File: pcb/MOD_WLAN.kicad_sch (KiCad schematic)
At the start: 8 parts, among them IC2 ESP32-C6-WROOM-1-N8, SW1 SW_DIP_x01

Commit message: updated wlan
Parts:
- added JP4, JP5: SolderJumper_2_Open, Jumper:SolderJumper-2_P1.3mm_Open_RoundedPad1.0x1.5mm, symbol Jumper:SolderJumper_2_Open
- added R53, R54: 100R, Resistor_SMD:R_0603_1608Metric_Pad0.98x0.95mm_HandSolder, symbol Device:R
- added R57: 10k, Resistor_SMD:R_0603_1608Metric_Pad0.98x0.95mm_HandSolder, symbol Device:R
- added R58, R59, R60, R72: 22R, Resistor_SMD:R_0603_1608Metric_Pad0.98x0.95mm_HandSolder, symbol Device:R
- added TP16: WLAN_EN, TestPoint:TestPoint_THTPad_D2.0mm_Drill1.0mm, symbol Connector:TestPoint
- added TP17: WLAN_BOOT, TestPoint:TestPoint_THTPad_D2.0mm_Drill1.0mm, symbol Connector:TestPoint
- C50: value 10u -> 22uF
- R47: value 100k -> 10k
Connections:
- net 3V3: now also R57.1
- net ESP_BOOT: now also JP5.1 (A); no longer IC2.15 (IO9), R47.2
- net ESP_EN: now also JP4.1 (A); no longer C48.1, IC2.3 (EN), R48.2, SW1.1
- net ESP_RX: now also R54.2; no longer IC2.24 (RXD0)
- net ESP_SPI_CLK: now also R58.1; no longer IC2.6 (IO6)
- net ESP_SPI_CS: now also R57.2, R60.1; no longer IC2.16 (IO18)
- net ESP_SPI_MISO: now also R72.2; no longer IC2.27 (IO2)
- net ESP_SPI_MOSI: now also R59.1; no longer IC2.7 (IO7)
- net ESP_TX: now also R53.2; no longer IC2.25 (TXD0)
- new net: IC2.24 (RXD0), R53.1
- new net: IC2.7 (IO7), R59.2
- new net: C48.1, IC2.3 (EN), JP4.2 (B), R48.2, SW1.1, TP16.1
- new net: IC2.6 (IO6), R58.2
- new net: IC2.15 (IO9), JP5.2 (B), R47.2, TP17.1
- new net: IC2.25 (TXD0), R54.1
- new net: IC2.16 (IO18), R60.2
- new net: IC2.27 (IO2), R72.1
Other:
- moved on the sheet: R49

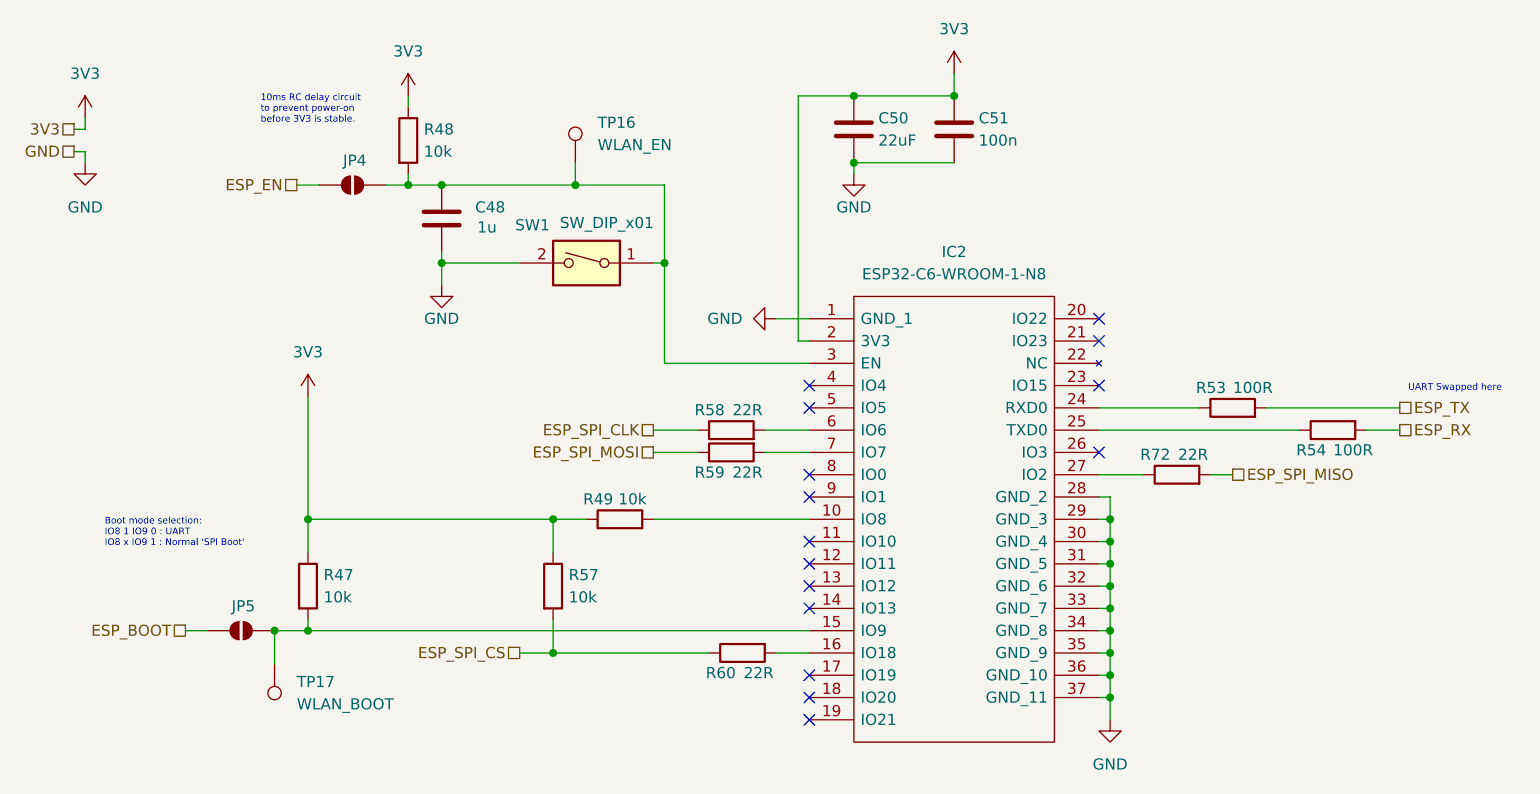
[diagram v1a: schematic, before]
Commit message: reannotated, updated some symbols
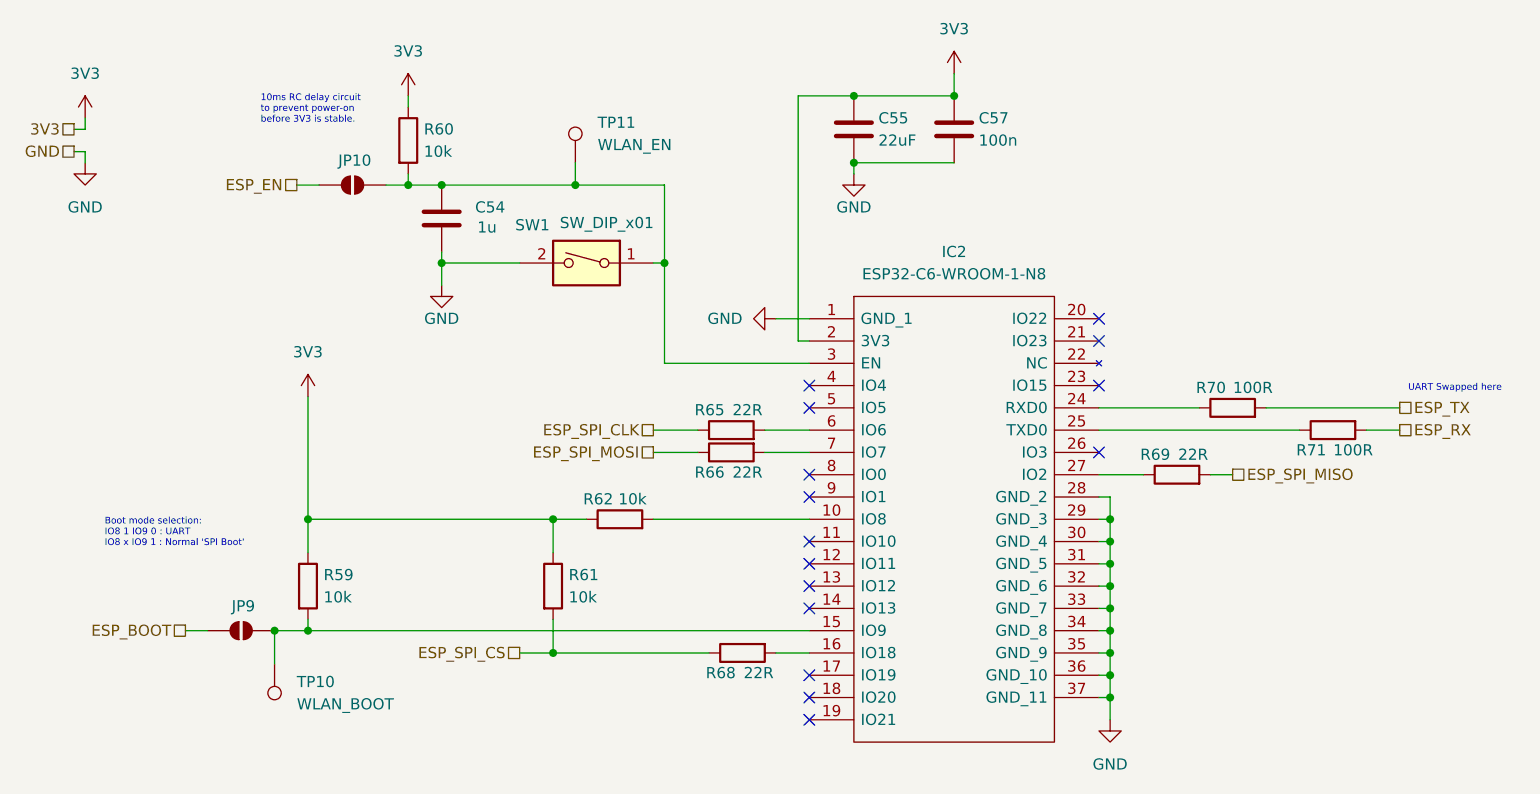
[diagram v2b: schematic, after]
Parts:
- renumbered C48 to C54, C50 to C55, C51 to C57, JP4 to JP10, JP5 to JP9, R47 to R59, R48 to R60, R57 to R61, R49 to R62, R58 to R65, R59 to R66, R60 to R68, R72 to R69, R53 to R70, R54 to R71, TP17 to TP10, TP16 to TP11
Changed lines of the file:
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@@
 		(on_board yes)
 		(dnp no)
-		(property "Reference" "R53"
+		(property "Reference" "R70"
 			(at 156.718 54.864 90)
 			(effects
@@
 			(project "NCU"
 				(path "/3aee14c3-5480-4f7c-989e-3fef81779034/0cdbc80d-6682-4488-acea-b93c92a9f88d"
-					(reference "R53")
+					(reference "R70")
 					(unit 1)
 				)
@@
 		(on_board yes)
 		(dnp no)
-		(property "Reference" "R59"
+		(property "Reference" "R66"
 			(at 99.568 64.516 90)
 			(effects
@@
 			(project "NCU"
 				(path "/3aee14c3-5480-4f7c-989e-3fef81779034/0cdbc80d-6682-4488-acea-b93c92a9f88d"
-					(reference "R59")
+					(reference "R66")
 					(unit 1)
 				)
@@
 		(on_board yes)
 		(dnp no)
-		(property "Reference" "R49"
+		(property "Reference" "R62"
 			(at 86.868 67.564 90)
 			(effects
@@
 			(project "NCU"
 				(path "/3aee14c3-5480-4f7c-989e-3fef81779034/0cdbc80d-6682-4488-acea-b93c92a9f88d"
-					(reference "R49")
+					(reference "R62")
 					(unit 1)
 				)
@@
 		(on_board yes)
 		(dnp no)
-		(property "Reference" "#PWR0218"
+		(property "Reference" "#PWR0286"
 			(at 114.3 36.83 0)
 			(effects
@@
 			(project "NCU"
 				(path "/3aee14c3-5480-4f7c-989e-3fef81779034/0cdbc80d-6682-4488-acea-b93c92a9f88d"
-					(reference "#PWR0218")
+					(reference "#PWR0286")
 					(unit 1)
 				)
@@
 		(on_board yes)
 		(dnp no)
-		(property "Reference" "R48"
+		(property "Reference" "R60"
 			(at 65.278 25.4 0)
 			(effects
@@
 			(project "NCU"
 				(path "/3aee14c3-5480-4f7c-989e-3fef81779034/0cdbc80d-6682-4488-acea-b93c92a9f88d"
-					(reference "R48")
+					(reference "R60")
 					(unit 1)
 				)
@@
 		(dnp no)
 		(fields_autoplaced yes)
-		(property "Reference" "#PWR0209"
+		(property "Reference" "#PWR0278"
 			(at 26.67 27.94 0)
 			(effects
@@
 			(project "NCU"
 				(path "/3aee14c3-5480-4f7c-989e-3fef81779034/0cdbc80d-6682-4488-acea-b93c92a9f88d"
-					(reference "#PWR0209")
+					(reference "#PWR0278")
 					(unit 1)
 				)
@@
 		(on_board yes)
 		(dnp no)
-		(property "Reference" "R58"
+		(property "Reference" "R65"
 			(at 99.568 57.404 90)
 			(effects
@@
 			(project "NCU"
 				(path "/3aee14c3-5480-4f7c-989e-3fef81779034/0cdbc80d-6682-4488-acea-b93c92a9f88d"
-					(reference "R58")
+					(reference "R65")
 					(unit 1)
 				)
@@
 		(on_board yes)
 		(dnp no)
-		(property "Reference" "R47"
+		(property "Reference" "R59"
 			(at 53.848 76.2 0)
 			(effects
@@
 			(project "NCU"
 				(path "/3aee14c3-5480-4f7c-989e-3fef81779034/0cdbc80d-6682-4488-acea-b93c92a9f88d"
-					(reference "R47")
+					(reference "R59")
 					(unit 1)
 				)
@@
 		(on_board yes)
 		(dnp no)
-		(property "Reference" "R54"
+		(property "Reference" "R71"
 			(at 168.148 61.976 90)
 			(effects
@@
 			(project "NCU"
 				(path "/3aee14c3-5480-4f7c-989e-3fef81779034/0cdbc80d-6682-4488-acea-b93c92a9f88d"
-					(reference "R54")
+					(reference "R71")
 					(unit 1)
 				)
@@
 		(dnp no)
 		(fields_autoplaced yes)
-		(property "Reference" "TP16"
+		(property "Reference" "TP11"
 			(at 85.09 24.6379 0)
 			(effects
@@
 			(project "NCU"
 				(path "/3aee14c3-5480-4f7c-989e-3fef81779034/0cdbc80d-6682-4488-acea-b93c92a9f88d"
-					(reference "TP16")
+					(reference "TP11")
 					(unit 1)
 				)
@@
 		(on_board yes)
 		(dnp no)
-		(property "Reference" "JP4"
+		(property "Reference" "JP10"
 			(at 57.404 28.956 0)
 			(effects
@@
 			(project ""
 				(path "/3aee14c3-5480-4f7c-989e-3fef81779034/0cdbc80d-6682-4488-acea-b93c92a9f88d"
-					(reference "JP4")
+					(reference "JP10")
 					(unit 1)
 				)
@@
 		(on_board yes)
 		(dnp no)
-		(property "Reference" "C48"
+		(property "Reference" "C54"
 			(at 71.12 34.2899 0)
 			(effects
@@
 			(project ""
 				(path "/3aee14c3-5480-4f7c-989e-3fef81779034/0cdbc80d-6682-4488-acea-b93c92a9f88d"
-					(reference "C48")
+					(reference "C54")
 					(unit 1)
 				)
@@
 		(dnp no)
 		(fields_autoplaced yes)
-		(property "Reference" "#PWR0219"
+		(property "Reference" "#PWR0288"
 			(at 125.73 22.86 0)
 			(effects
@@
 			(project "NCU"
 				(path "/3aee14c3-5480-4f7c-989e-3fef81779034/0cdbc80d-6682-4488-acea-b93c92a9f88d"
-					(reference "#PWR0219")
+					(reference "#PWR0288")
 					(unit 1)
 				)
@@
 		(dnp no)
 		(fields_autoplaced yes)
-		(property "Reference" "#PWR0213"
+		(property "Reference" "#PWR0282"
 			(at 63.5 25.4 0)
 			(effects
@@
 			(project "NCU"
 				(path "/3aee14c3-5480-4f7c-989e-3fef81779034/0cdbc80d-6682-4488-acea-b93c92a9f88d"
-					(reference "#PWR0213")
+					(reference "#PWR0282")
 					(unit 1)
 				)
@@
 		(dnp no)
 		(fields_autoplaced yes)
-		(property "Reference" "#PWR0220"
+		(property "Reference" "#PWR0291"
 			(at 143.51 99.06 0)
 			(effects
@@
 			(project "NCU"
 				(path "/3aee14c3-5480-4f7c-989e-3fef81779034/0cdbc80d-6682-4488-acea-b93c92a9f88d"
-					(reference "#PWR0220")
+					(reference "#PWR0291")
 					(unit 1)
 				)
@@
 		(dnp no)
 		(fields_autoplaced yes)
-		(property "Reference" "TP17"
+		(property "Reference" "TP10"
 			(at 50.8 88.3919 0)
 			(effects
@@
 			(project "NCU"
 				(path "/3aee14c3-5480-4f7c-989e-3fef81779034/0cdbc80d-6682-4488-acea-b93c92a9f88d"
-					(reference "TP17")
+					(reference "TP10")
 					(unit 1)
 				)
@@
 		(on_board yes)
 		(dnp no)
-		(property "Reference" "C50"
+		(property "Reference" "C55"
 			(at 117.094 24.13 0)
 			(effects
@@
 			(project "NCU"
 				(path "/3aee14c3-5480-4f7c-989e-3fef81779034/0cdbc80d-6682-4488-acea-b93c92a9f88d"
-					(reference "C50")
+					(reference "C55")
 					(unit 1)
 				)
@@
 		(dnp no)
 		(fields_autoplaced yes)
-		(property "Reference" "#PWR0216"
+		(property "Reference" "#PWR0285"
 			(at 99.06 46.99 0)
 			(effects
@@
 			(project "NCU"
 				(path "/3aee14c3-5480-4f7c-989e-3fef81779034/0cdbc80d-6682-4488-acea-b93c92a9f88d"
-					(reference "#PWR0216")
+					(reference "#PWR0285")
 					(unit 1)
 				)
@@
 		(on_board yes)
 		(dnp no)
-		(property "Reference" "#PWR0214"
+		(property "Reference" "#PWR0283"
 			(at 67.31 49.53 0)
 			(effects
@@
 			(project "NCU"
 				(path "/3aee14c3-5480-4f7c-989e-3fef81779034/0cdbc80d-6682-4488-acea-b93c92a9f88d"
-					(reference "#PWR0214")
+					(reference "#PWR0283")
 					(unit 1)
 				)
@@
 		(on_board yes)
 		(dnp no)
-		(property "Reference" "R60"
+		(property "Reference" "R68"
 			(at 100.838 87.376 90)
 			(effects
@@
 			(project "NCU"
 				(path "/3aee14c3-5480-4f7c-989e-3fef81779034/0cdbc80d-6682-4488-acea-b93c92a9f88d"
-					(reference "R60")
+					(reference "R68")
 					(unit 1)
 				)
@@
 		(on_board yes)
 		(dnp no)
-		(property "Reference" "R57"
+		(property "Reference" "R61"
 			(at 81.788 76.2 0)
 			(effects
@@
 			(project "NCU"
 				(path "/3aee14c3-5480-4f7c-989e-3fef81779034/0cdbc80d-6682-4488-acea-b93c92a9f88d"
-					(reference "R57")
+					(reference "R61")
 					(unit 1)
 				)
@@
 		(dnp no)
 		(fields_autoplaced yes)
-		(property "Reference" "#PWR0212"
+		(property "Reference" "#PWR0281"
 			(at 52.07 59.69 0)
 			(effects
@@
 			(project "NCU"
 				(path "/3aee14c3-5480-4f7c-989e-3fef81779034/0cdbc80d-6682-4488-acea-b93c92a9f88d"
-					(reference "#PWR0212")
+					(reference "#PWR0281")
 					(unit 1)
 				)
@@
 		(on_board yes)
 		(dnp no)
-		(property "Reference" "R72"
+		(property "Reference" "R69"
 			(at 150.368 62.484 90)
 			(effects
@@
 			(project "NCU"
 				(path "/3aee14c3-5480-4f7c-989e-3fef81779034/0cdbc80d-6682-4488-acea-b93c92a9f88d"
-					(reference "R72")
+					(reference "R69")
 					(unit 1)
 				)
@@
 		(on_board yes)
 		(dnp no)
-		(property "Reference" "JP5"
+		(property "Reference" "JP9"
 			(at 44.704 79.756 0)
 			(effects
@@
 			(project "NCU"
 				(path "/3aee14c3-5480-4f7c-989e-3fef81779034/0cdbc80d-6682-4488-acea-b93c92a9f88d"
-					(reference "JP5")
+					(reference "JP9")
 					(unit 1)
 				)
@@
 		(dnp no)
 		(fields_autoplaced yes)
-		(property "Reference" "#PWR0211"
+		(property "Reference" "#PWR0280"
 			(at 26.67 35.56 0)
 			(effects
@@
 			(project "NCU"
 				(path "/3aee14c3-5480-4f7c-989e-3fef81779034/0cdbc80d-6682-4488-acea-b93c92a9f88d"
-					(reference "#PWR0211")
+					(reference "#PWR0280")
 					(unit 1)
 				)
@@
 		(on_board yes)
 		(dnp no)
-		(property "Reference" "C51"
+		(property "Reference" "C57"
 			(at 128.524 24.13 0)
 			(effects
@@
 			(project "NCU"
 				(path "/3aee14c3-5480-4f7c-989e-3fef81779034/0cdbc80d-6682-4488-acea-b93c92a9f88d"
-					(reference "C51")
-					(unit 1)
-				)
+					(reference "C57")
+					(unit 1)
+				)

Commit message: minor changes before layout
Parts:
- added TP21: ESP_TX, TestPoint:TestPoint_THTPad_D2.0mm_Drill1.0mm, symbol Connector:TestPoint
- added TP22: ESP_RX, TestPoint:TestPoint_THTPad_D2.0mm_Drill1.0mm, symbol Connector:TestPoint
- C55: value 22uF -> 47uF
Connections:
- net ESP_RX: now also TP22.1
- net ESP_TX: now also TP21.1
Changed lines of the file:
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@@
+	)
+	(junction
+		(at 175.26 57.15)
+		(diameter 0)
+		(color 0 0 0 0)
 	)
 	(junction
@@
 	)
 	(junction
+		(at 175.26 59.69)
+		(diameter 0)
+		(color 0 0 0 0)
+	)
+	(junction
 		(at 143.51 87.63)
 		(diameter 0)
@@
 	(wire
 		(pts
+			(xy 175.26 53.34) (xy 175.26 57.15)
+		)
+		(stroke
+			(width 0)
+			(type default)
+		)
+	)
+	(wire
+		(pts
 			(xy 63.5 21.59) (xy 63.5 22.86)
 		)
@@
 	(wire
 		(pts
-			(xy 172.72 59.69) (xy 176.53 59.69)
+			(xy 172.72 59.69) (xy 175.26 59.69)
 		)
 		(stroke
@@
 	(wire
 		(pts
+			(xy 175.26 59.69) (xy 176.53 59.69)
+		)
+		(stroke
+			(width 0)
+			(type default)
+		)
+	)
+	(wire
+		(pts
 			(xy 142.24 57.15) (xy 153.67 57.15)
 		)
@@
 	(wire
 		(pts
+			(xy 175.26 57.15) (xy 176.53 57.15)
+		)
+		(stroke
+			(width 0)
+			(type default)
+		)
+	)
+	(wire
+		(pts
 			(xy 52.07 69.85) (xy 52.07 73.66)
 		)
@@
 	(wire
 		(pts
-			(xy 161.29 57.15) (xy 176.53 57.15)
+			(xy 161.29 57.15) (xy 175.26 57.15)
 		)
 		(stroke
@@
 		(pts
 			(xy 67.31 31.75) (xy 82.55 31.75)
+		)
+		(stroke
+			(width 0)
+			(type default)
+		)
+	)
+	(wire
+		(pts
+			(xy 175.26 59.69) (xy 175.26 62.23)
 		)
 		(stroke
@@
 			)
 		)
-		(property "Value" "22uF"
+		(property "Value" "47uF"
 			(at 117.094 26.67 0)
 			(effects
@@
 	)
 	(symbol
+		(lib_id "Connector:TestPoint")
+		(at 175.26 62.23 0)
+		(mirror x)
+		(unit 1)
+		(exclude_from_sim no)
+		(in_bom yes)
+		(on_board yes)
+		(dnp no)
+		(property "Reference" "TP22"
+			(at 177.8 66.8021 0)
+			(effects
+				(font
+					(size 1.27 1.27)
+				)
+				(justify left)
+			)
+		)
+		(property "Value" "ESP_RX"
+			(at 177.8 64.2621 0)
+			(effects
+				(font
+					(size 1.27 1.27)
+				)
+				(justify left)
+			)
+		)
+		(property "Footprint" "TestPoint:TestPoint_THTPad_D2.0mm_Drill1.0mm"
+			(at 180.34 62.23 0)
+			(effects
+				(font
+					(size 1.27 1.27)
+				)
+				(hide yes)
+			)
+		)
+		(property "Datasheet" "~"
+			(at 180.34 62.23 0)
+			(effects
+				(font
+					(size 1.27 1.27)
+				)
+				(hide yes)
+			)
+		)
+		(property "Description" "test point"
+			(at 175.26 62.23 0)
+			(effects
+				(font
+					(size 1.27 1.27)
+				)
+				(hide yes)
+			)
+		)
+		(pin "1"
+		)
+		(instances
+			(project "NCU"
+				(path "/3aee14c3-5480-4f7c-989e-3fef81779034/0cdbc80d-6682-4488-acea-b93c92a9f88d"
+					(reference "TP22")
+					(unit 1)
+				)
+			)
+		)
+	)
+	(symbol
 		(lib_id "Device:R")
 		(at 80.01 77.47 0)
@@
 					(unit 1)
 				)
+			)
+		)
+	)
+	(symbol
+		(lib_id "Connector:TestPoint")
+		(at 175.26 53.34 0)
+		(unit 1)
+		(exclude_from_sim no)
+		(in_bom yes)
+		(on_board yes)
+		(dnp no)
+		(fields_autoplaced yes)
+		(property "Reference" "TP21"
+			(at 177.8 48.7679 0)
+			(effects
+				(font
+					(size 1.27 1.27)
+				)
+				(justify left)
+			)
+		)
+		(property "Value" "ESP_TX"
+			(at 177.8 51.3079 0)
+			(effects
+				(font
+					(size 1.27 1.27)
+				)
+				(justify left)
+			)
+		)
+		(property "Footprint" "TestPoint:TestPoint_THTPad_D2.0mm_Drill1.0mm"
+			(at 180.34 53.34 0)
+			(effects
+				(font
+					(size 1.27 1.27)
+				)
+				(hide yes)
+			)
+		)
+		(property "Datasheet" "~"
+			(at 180.34 53.34 0)
+			(effects
+				(font
+					(size 1.27 1.27)
+				)
+				(hide yes)
+			)
+		)
+		(property "Description" "test point"
+			(at 175.26 53.34 0)
+			(effects
+				(font
+					(size 1.27 1.27)
+				)
+				(hide yes)
+			)
+		)
+		(pin "1"
+		)
+		(instances
+			(project "NCU"
+				(path "/3aee14c3-5480-4f7c-989e-3fef81779034/0cdbc80d-6682-4488-acea-b93c92a9f88d"
+					(reference "TP21")
+					(unit 1)
+				)

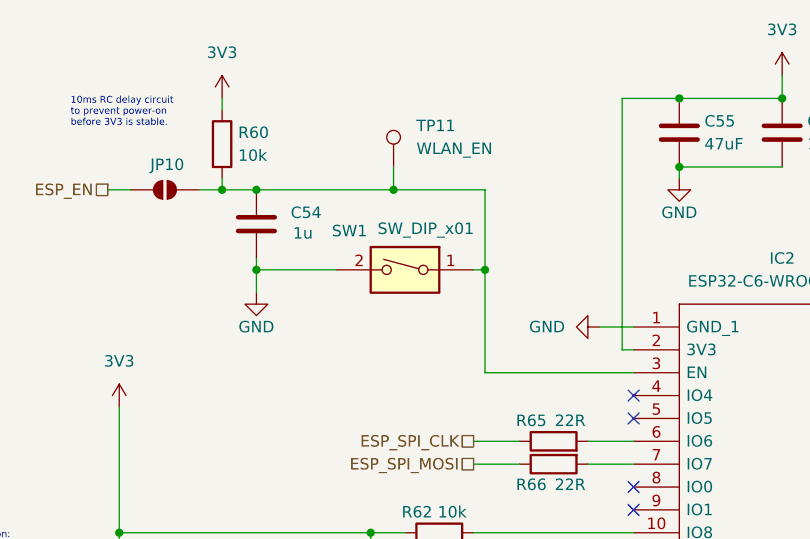
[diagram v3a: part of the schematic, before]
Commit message: laid out most of esp
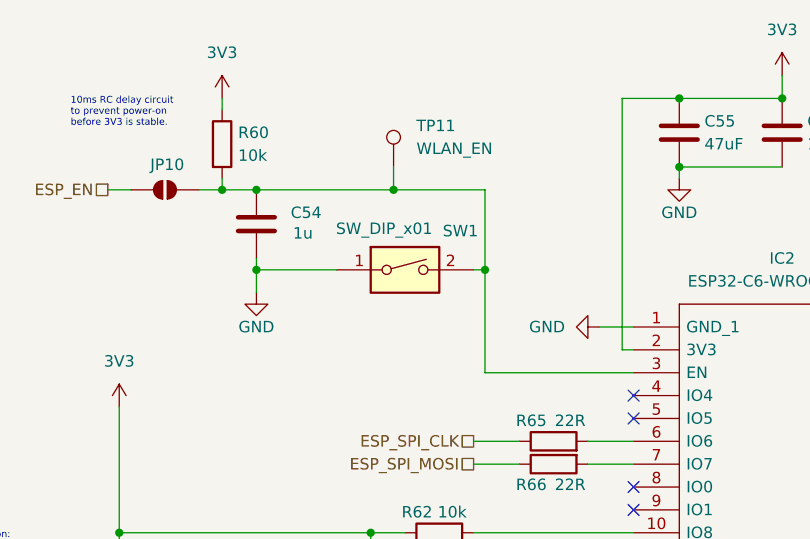
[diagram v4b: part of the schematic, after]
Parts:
- SW1: footprint SamacSys_Parts:DS01254L01BE -> SamacSys_Parts:EDS01SGNNTR04Q
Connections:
- net GND: now also SW1.1; no longer SW1.2
- net at C54.1, IC2.3 (EN), JP10.2 (B)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: now also SW1.2; no longer SW1.1
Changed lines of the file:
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@@
 		(lib_id "Switch:SW_DIP_x01")
 		(at 83.82 40.64 0)
-		(mirror y)
 		(unit 1)
 		(exclude_from_sim no)
@@
 		(dnp no)
 		(property "Reference" "SW1"
-			(at 75.692 36.322 0)
+			(at 91.948 36.322 0)
 			(effects
 				(font
@@
 		)
 		(property "Value" "SW_DIP_x01"
-			(at 80.772 36.068 0)
+			(at 86.868 36.068 0)
 			(effects
 				(font
@@
 			)
 		)
-		(property "Footprint" "SamacSys_Parts:DS01254L01BE"
+		(property "Footprint" "SamacSys_Parts:EDS01SGNNTR04Q"
 			(at 83.82 40.64 0)
 			(effects
